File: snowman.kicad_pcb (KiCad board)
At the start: 2 copper layers, 38.4 x 70.7 mm, 13 parts, among them SW1 SW_SPST, SW2 SW_SPST, SW3 SW_SPST, U1 ATTINY85-20SU

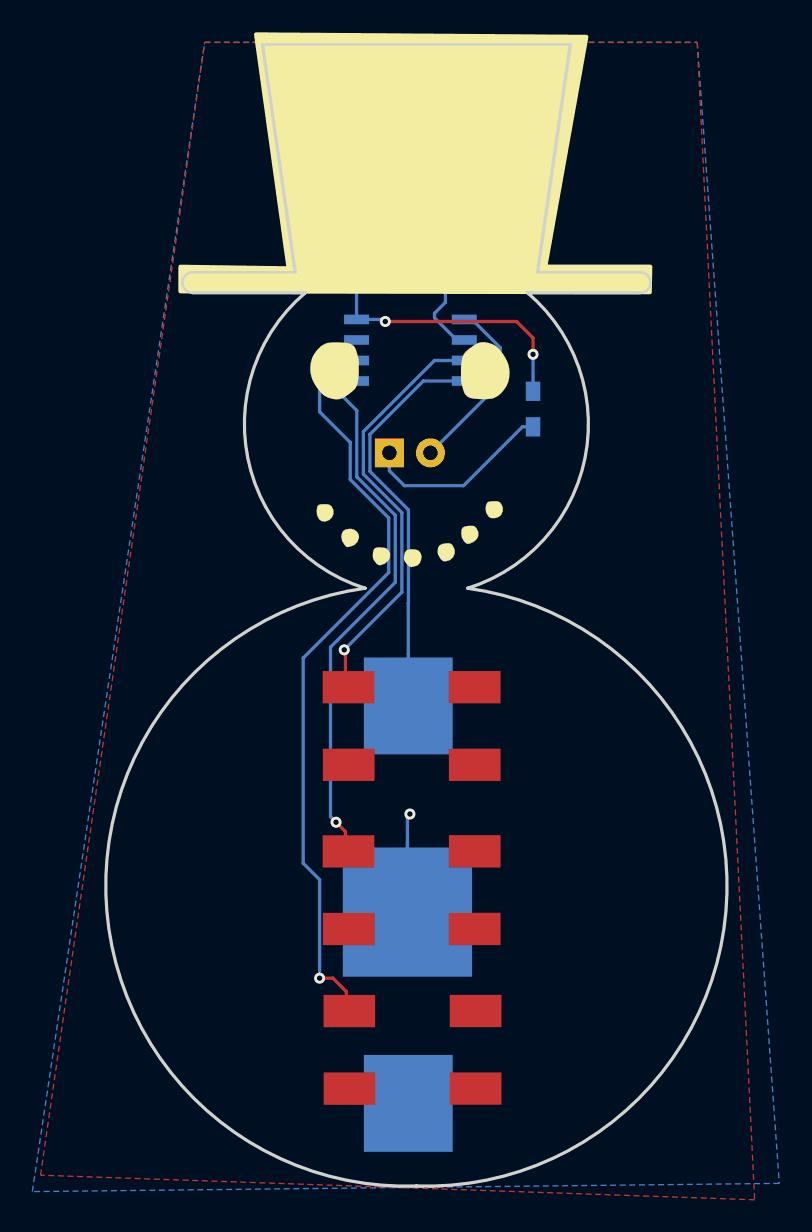
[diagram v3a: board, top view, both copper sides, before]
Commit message: Shink VCC Copper Zone
Shrink VCC copper zone on back of board so any possible scratches on PCB won't make contact with negative side of battery
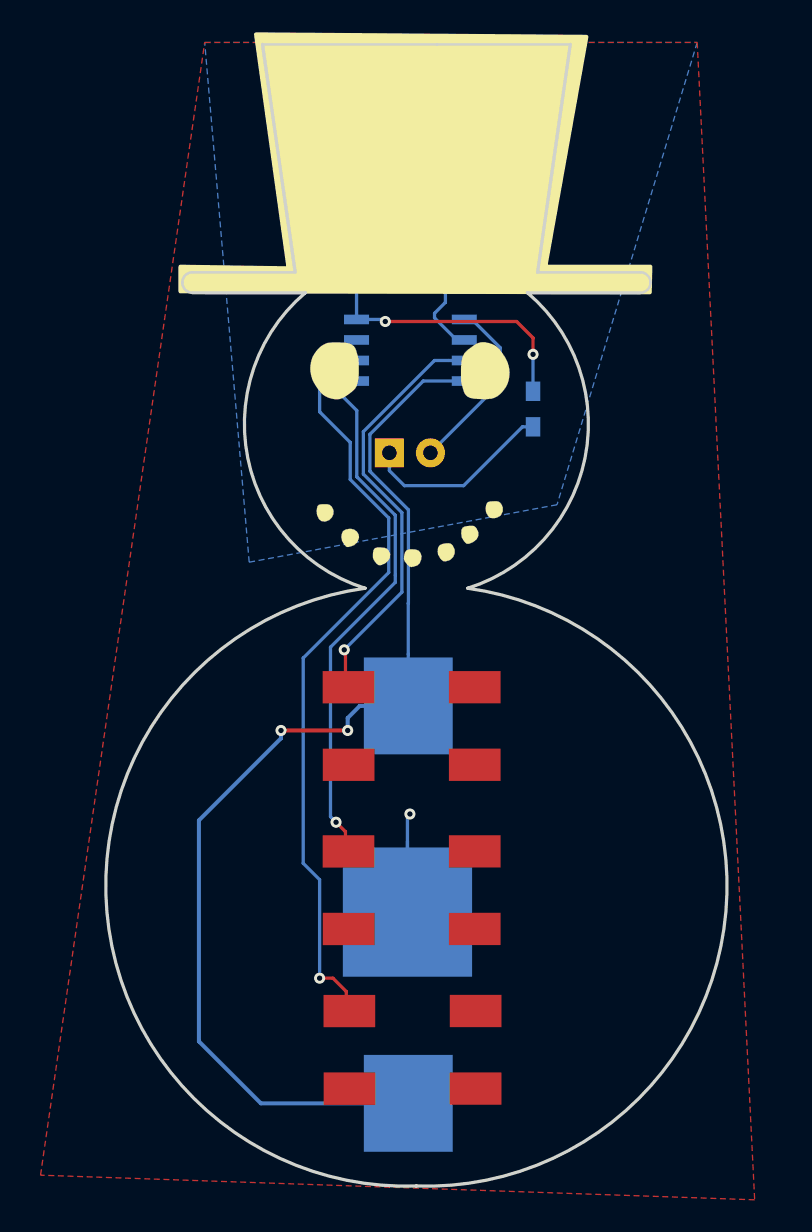
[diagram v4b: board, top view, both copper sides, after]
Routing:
- net /VCC: track 25.0 -> 69.9 mm, vias 0 -> 2
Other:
- net class Default: trace_width 0.2032 -> 0.25
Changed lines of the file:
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@@
-(kicad_pcb (version 20170123) (host pcbnew no-vcs-found-0633d90~59~ubuntu16.04.1)
+(kicad_pcb (version 20170123) (host pcbnew no-vcs-found-1fe91e6~59~ubuntu16.04.1)
   (general
     (thickness 1.6)
     (drawings 18)
-    (tracks 84)
+    (tracks 95)
     (zones 0)
     (modules 13)
@@
     (34 B.Paste user)
     (35 F.Paste user)
-    (36 B.SilkS user)
+    (36 B.SilkS user hide)
     (37 F.SilkS user)
-    (38 B.Mask user)
+    (38 B.Mask user hide)
     (39 F.Mask user)
     (40 Dwgs.User user)
@@
   )
   (setup
-    (last_trace_width 0.2032)
+    (last_trace_width 0.25)
     (trace_clearance 0.2032)
     (zone_clearance 0.508)
@@
       (layerselection 0x010f0_ffffffff)
       (usegerberextensions true)
+      (usegerberattributes true)
+      (usegerberadvancedattributes true)
+      (creategerberjobfile true)
       (excludeedgelayer true)
       (linewidth 0.100000)
@@
   (net_class Default "This is the default net class."
     (clearance 0.2032)
-    (trace_width 0.2032)
+    (trace_width 0.25)
     (via_dia 0.6858)
     (via_drill 0.3302)
     (uvia_dia 0.762)
     (uvia_drill 0.508)
-    (diff_pair_gap 0.25)
-    (diff_pair_width 0.2032)
     (add_net /VCC)
     (add_net GND)
@@
   (via (at 160.02 99.568) (size 0.6858) (drill 0.3302) (layers F.Cu B.Cu) (net 1))
   (segment (start 159.8676 99.7204) (end 160.02 99.568) (width 0.2032) (layer B.Cu) (net 1))
+  (segment (start 146.962436 113.638583) (end 150.798853 117.475) (width 0.25) (layer B.Cu) (net 2))
+  (segment (start 150.798853 117.475) (end 159.9184 117.475) (width 0.25) (layer B.Cu) (net 2))
+  (segment (start 146.962436 99.963016) (end 146.962436 113.638583) (width 0.25) (layer B.Cu) (net 2))
+  (segment (start 152.042436 94.398083) (end 152.042436 94.883016) (width 0.25) (layer B.Cu) (net 2))
+  (segment (start 152.042436 94.883016) (end 146.962436 99.963016) (width 0.25) (layer B.Cu) (net 2))
+  (segment (start 156.169936 94.398083) (end 152.042436 94.398083) (width 0.25) (layer F.Cu) (net 2))
+  (via (at 152.042436 94.398083) (size 0.6858) (drill 0.3302) (layers F.Cu B.Cu) (net 2))
+  (segment (start 159.9184 92.8786) (end 156.9184 92.8786) (width 0.25) (layer B.Cu) (net 2))
+  (segment (start 156.9184 92.8786) (end 156.169936 93.627064) (width 0.25) (layer B.Cu) (net 2))
+  (segment (start 156.169936 93.627064) (end 156.169936 94.398083) (width 0.25) (layer B.Cu) (net 2))
+  (via (at 156.169936 94.398083) (size 0.6858) (drill 0.3302) (layers F.Cu B.Cu) (net 2))
   (segment (start 157.545199 78.359841) (end 159.928848 80.74349) (width 0.2032) (layer B.Cu) (net 2))
   (segment (start 157.545199 76.072159) (end 157.545199 78.359841) (width 0.2032) (layer B.Cu) (net 2))
@@
     (polygon
       (pts
-        (xy 147.32 51.816) (xy 177.8 51.816) (xy 182.88 122.428) (xy 136.652 122.936)
+        (xy 147.32 51.816) (xy 177.8 51.816) (xy 169.123936 80.428083) (xy 150.073936 83.984083)
       )
     )
